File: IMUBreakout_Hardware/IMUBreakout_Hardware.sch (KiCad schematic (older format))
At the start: 6 parts

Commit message: Fixed PCB, added BOM
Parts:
- gave numbers to parts that had none: 2
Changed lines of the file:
@@
 	6340 2360 470  2360
 $Comp
-L MRDT_Connectors:Molex_SL_04 Conn?
+L MRDT_Connectors:Molex_SL_04 Conn1
 U 1 1 5C7ACAF9
 P 5200 1450
-F 0 "Conn?" H 5327 1708 60  0000 L CNN
+F 0 "Conn1" H 5327 1708 60  0000 L CNN
 F 1 "Molex_SL_04" H 5327 1602 60  0000 L CNN
 F 2 "MRDT_Connectors:MOLEX_SL_04_Horizontal" H 5200 1450 60  0001 C CNN
@@
 	5000 1400 4950 1400
 $Comp
-L MRDT_Sensors:Razor_9DOF_Sparkfun U?
+L MRDT_Sensors:Razor_9DOF_Sparkfun U1
 U 1 1 5C7ACFCA
 P 3600 2000
-F 0 "U?" H 3800 2965 50  0000 C CNN
+F 0 "U1" H 3800 2965 50  0000 C CNN
 F 1 "Razor_9DOF_Sparkfun" H 3800 2874 50  0000 C CNN
 F 2 "MRDT_Sensors:Razor_9DOF_Sparkfun" H 3350 2250 50  0001 C CNN

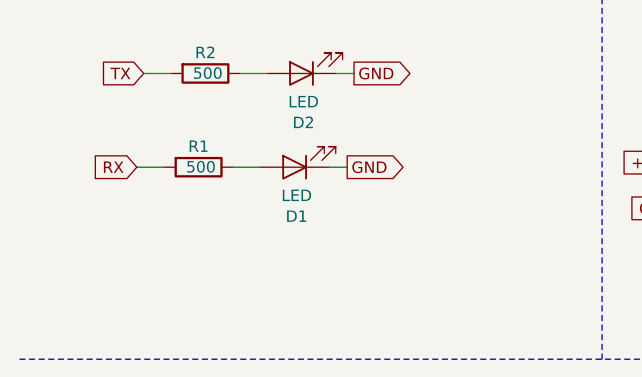
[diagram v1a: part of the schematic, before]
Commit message: Expand board, Power LED
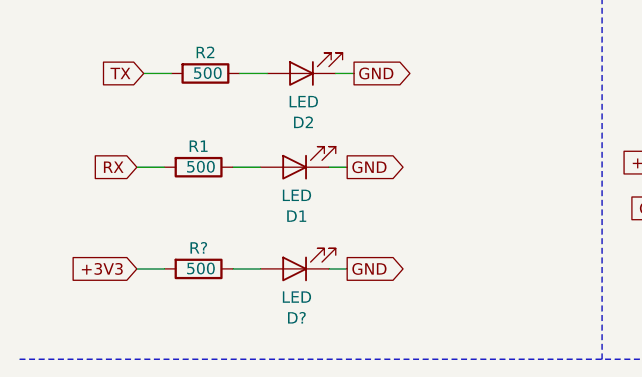
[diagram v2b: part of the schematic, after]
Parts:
- added D?: LED, LED_SMD:LED_0603_1608Metric_Pad1.05x0.95mm_HandSolder, symbol Device:LED
- added R?: 500, Resistor_SMD:R_0603_1608Metric_Pad1.05x0.95mm_HandSolder, symbol Device:R
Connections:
- net +3V3: now also R?.2
- net GND: now also D?.1 (K)
- new net: D?.2 (A), R?.1
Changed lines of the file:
@@
 Wire Wire Line
 	4100 1550 4150 1550
+Text GLabel 990  1965 0    50   Input ~ 0
++3V3
+$Comp
+L Device:R R?
+U 1 1 5C7EE240
+P 1260 1965
+F 0 "R?" V 1170 1965 50  0000 C CNN
+F 1 "500" V 1260 1975 50  0000 C CNN
+F 2 "Resistor_SMD:R_0603_1608Metric_Pad1.05x0.95mm_HandSolder" V 1190 1965 50  0001 C CNN
+F 3 "~" H 1260 1965 50  0001 C CNN
+	1    1260 1965
+	0    1    1    0
+$EndComp
+Wire Wire Line
+	1110 1965 990  1965
+$Comp
+L Device:LED D?
+U 1 1 5C7EE248
+P 1680 1965
+F 0 "D?" H 1671 2181 50  0000 C CNN
+F 1 "LED" H 1671 2090 50  0000 C CNN
+F 2 "LED_SMD:LED_0603_1608Metric_Pad1.05x0.95mm_HandSolder" H 1680 1965 50  0001 C CNN
+F 3 "~" H 1680 1965 50  0001 C CNN
+	1    1680 1965
+	-1   0    0    1
+$EndComp
+Wire Wire Line
+	1410 1965 1530 1965
+Wire Wire Line
+	1830 1965 1910 1965
+Text GLabel 1910 1965 2    50   Output ~ 0
+GND
 $EndSCHEMATC

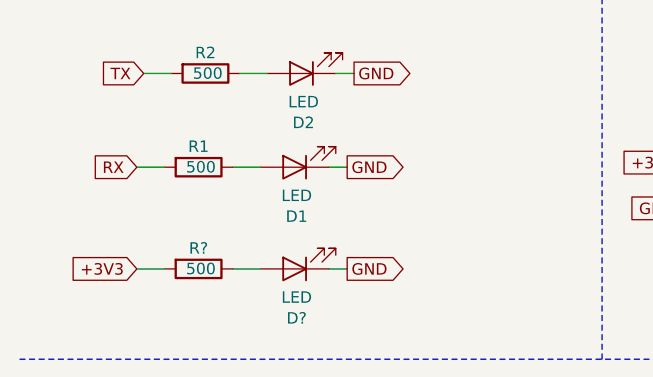
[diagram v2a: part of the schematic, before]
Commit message: Made zSilkscreen edits
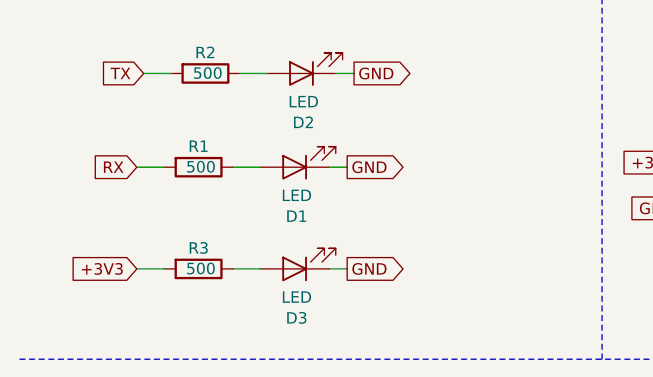
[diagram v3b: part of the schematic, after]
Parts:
- gave numbers to parts that had none: 2
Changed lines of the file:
@@
 +3V3
 $Comp
-L Device:R R?
+L Device:R R3
 U 1 1 5C7EE240
 P 1260 1965
-F 0 "R?" V 1170 1965 50  0000 C CNN
+F 0 "R3" V 1170 1965 50  0000 C CNN
 F 1 "500" V 1260 1975 50  0000 C CNN
 F 2 "Resistor_SMD:R_0603_1608Metric_Pad1.05x0.95mm_HandSolder" V 1190 1965 50  0001 C CNN
@@
 	1110 1965 990  1965
 $Comp
-L Device:LED D?
+L Device:LED D3
 U 1 1 5C7EE248
 P 1680 1965
-F 0 "D?" H 1671 2181 50  0000 C CNN
+F 0 "D3" H 1671 2181 50  0000 C CNN
 F 1 "LED" H 1671 2090 50  0000 C CNN
 F 2 "LED_SMD:LED_0603_1608Metric_Pad1.05x0.95mm_HandSolder" H 1680 1965 50  0001 C CNN
